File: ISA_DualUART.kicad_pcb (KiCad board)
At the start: 2 copper layers, 176.5 x 90.2 mm, 74 parts, among them J1 ISA BUS, J10 Parallel Port, J2 ADDR_IRQ, J3 UART1_SEL, J4 UART2_SEL, J6 Serial 2 IDC, J7 Serial 1 DB9, J9 Parport IRQ Select, U1 74LS138, U11 74LS30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

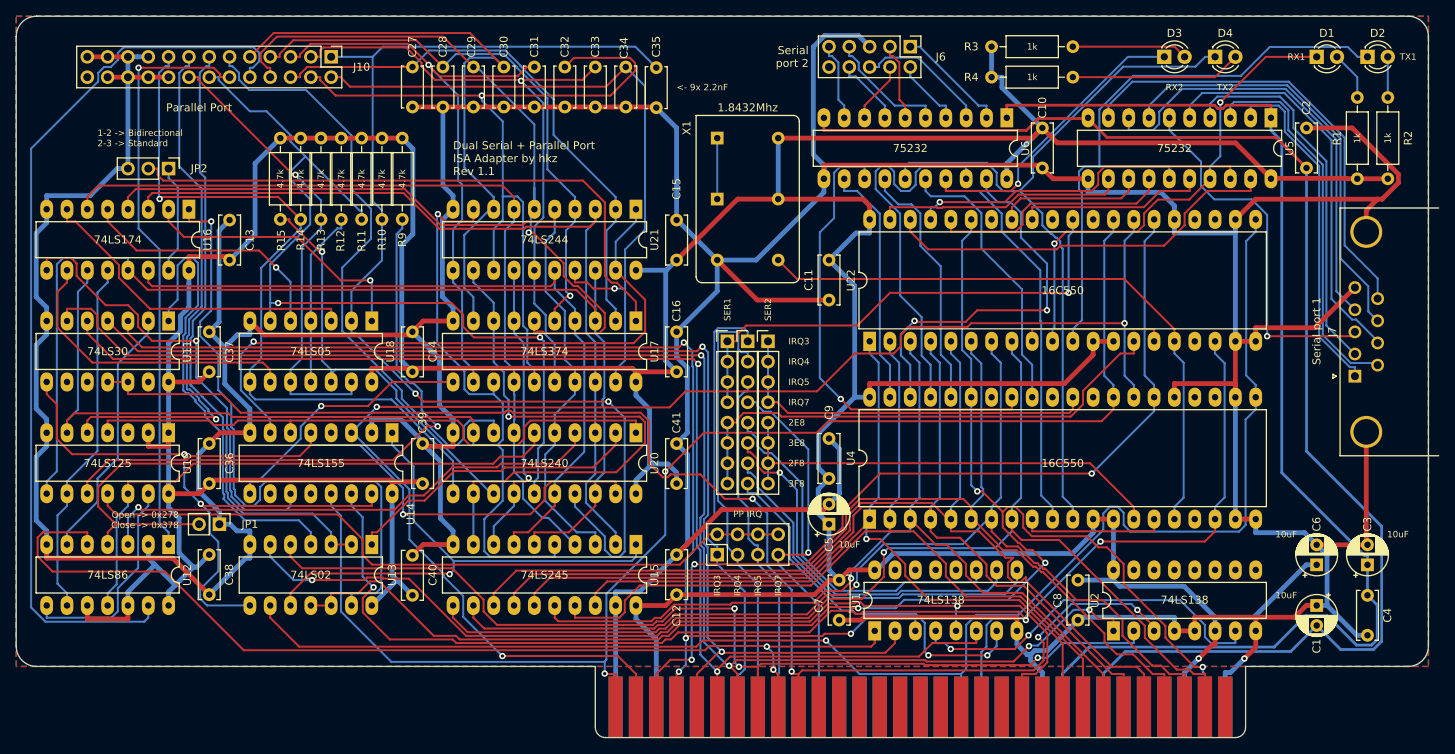
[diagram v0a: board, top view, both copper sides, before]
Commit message: Slightly better silkscreen
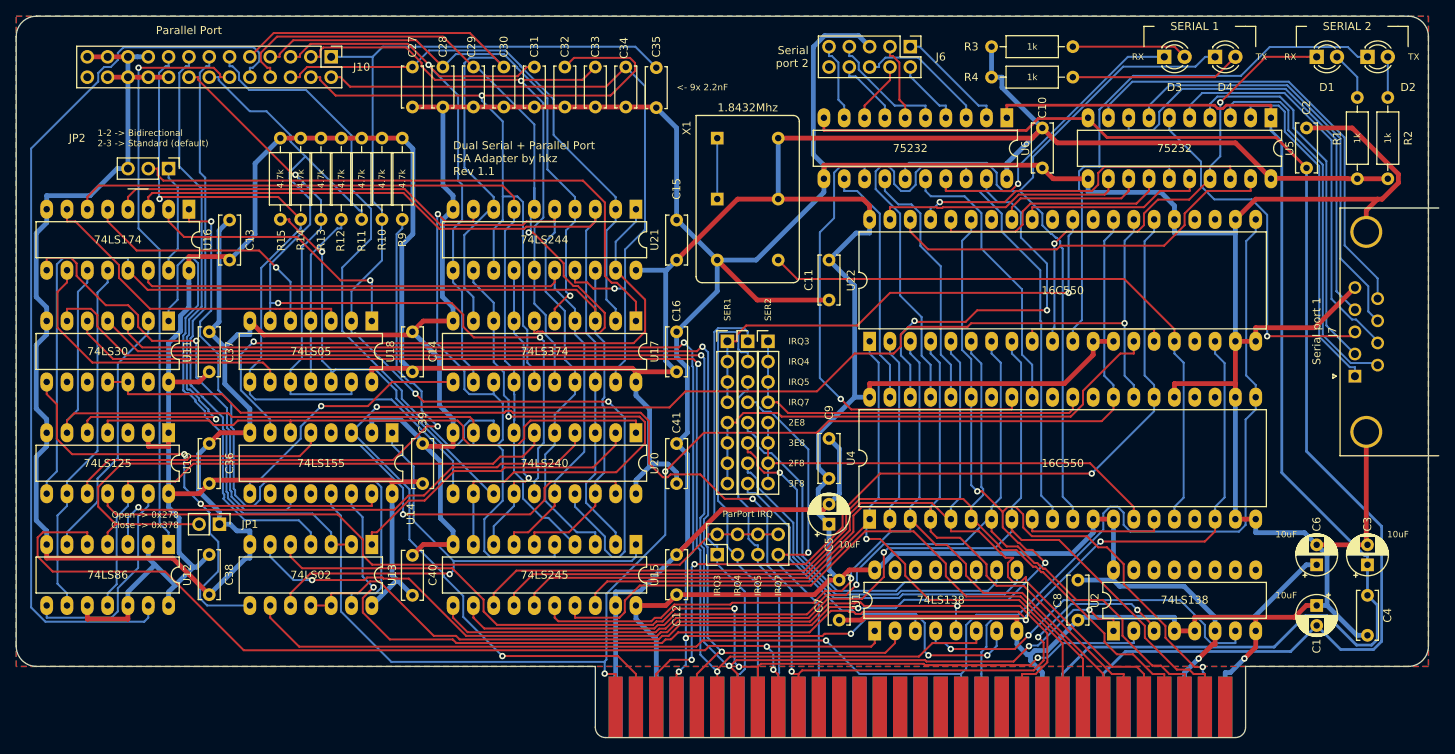
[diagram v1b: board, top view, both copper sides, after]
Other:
- board text added: "1-2 -> Bidirectional 2-3 -> Standard (default)"
- board text added: "ParPort IRQ"
- board text added: "RX"
- board text added: "SERIAL 1"
- board text added: "SERIAL 2"
- board text added: "TX"
- board text removed: "1-2 -> Bidirectional 2-3 -> Standard"
- board text removed: "PP IRQ"
- board text removed: "RX1"
- board text removed: "RX2"
- board text removed: "TX1"
- board text removed: "TX2"
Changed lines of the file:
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@@
   (general
     (thickness 1.6)
-    (drawings 76)
+    (drawings 89)
     (tracks 2452)
     (zones 0)
@@
   (page A3)
   (layers
-    (0 F.Cu signal)
-    (31 B.Cu signal)
+    (0 F.Cu signal hide)
+    (31 B.Cu signal hide)
     (32 B.Adhes user)
     (33 F.Adhes user)
@@
     (descr "Through hole straight pin header, 1x03, 2.54mm pitch, single row")
     (tags "Through hole pin header THT 1x03 2.54mm single row")
-    (fp_text reference JP2 (at 0 -3.81) (layer F.SilkS)
+    (fp_text reference JP2 (at -3.81 11.43) (layer F.SilkS)
       (effects (font (size 1 1) (thickness 0.15)))
     )
@@
     (descr "LED, diameter 3.0mm, 2 pins")
     (tags "LED diameter 3.0mm 2 pins")
-    (fp_text reference D4 (at 1.27 -2.96) (layer F.SilkS)
+    (fp_text reference D4 (at 1.27 3.81) (layer F.SilkS)
       (effects (font (size 1 1) (thickness 0.15)))
     )
@@
     (descr "LED, diameter 3.0mm, 2 pins")
     (tags "LED diameter 3.0mm 2 pins")
-    (fp_text reference D3 (at 1.27 -2.96) (layer F.SilkS)
+    (fp_text reference D3 (at 1.27 3.81) (layer F.SilkS)
       (effects (font (size 1 1) (thickness 0.15)))
     )
@@
     (descr "LED, diameter 3.0mm, 2 pins")
     (tags "LED diameter 3.0mm 2 pins")
-    (fp_text reference D2 (at 1.27 -2.96) (layer F.SilkS)
+    (fp_text reference D2 (at 5.08 3.81) (layer F.SilkS)
       (effects (font (size 1 1) (thickness 0.15)))
     )
@@
     (descr "LED, diameter 3.0mm, 2 pins")
     (tags "LED diameter 3.0mm 2 pins")
-    (fp_text reference D1 (at 1.27 -2.96) (layer F.SilkS)
+    (fp_text reference D1 (at 1.27 3.81) (layer F.SilkS)
       (effects (font (size 1 1) (thickness 0.15)))
     )
@@
     )
   )
+  (gr_line (start 152.4 134.62) (end 154.94 134.62) (layer F.SilkS) (width 0.12))
+  (gr_line (start 292.1 114.3) (end 290.83 114.3) (layer F.SilkS) (width 0.12))
+  (gr_line (start 311.15 114.3) (end 309.88 114.3) (layer F.SilkS) (width 0.12))
+  (gr_line (start 312.42 114.3) (end 311.15 114.3) (layer F.SilkS) (width 0.12))
+  (gr_line (start 312.42 116.84) (end 312.42 114.3) (layer F.SilkS) (width 0.12))
+  (gr_line (start 298.45 114.3) (end 299.72 114.3) (layer F.SilkS) (width 0.12))
+  (gr_line (start 298.45 116.84) (end 298.45 114.3) (layer F.SilkS) (width 0.12))
+  (gr_line (start 293.37 114.3) (end 292.1 114.3) (layer F.SilkS) (width 0.12))
+  (gr_line (start 293.37 116.84) (end 293.37 114.3) (layer F.SilkS) (width 0.12))
+  (gr_line (start 279.4 114.3) (end 280.67 114.3) (layer F.SilkS) (width 0.12))
+  (gr_line (start 279.4 116.84) (end 279.4 114.3) (layer F.SilkS) (width 0.12))
+  (gr_text "SERIAL 2" (at 304.8 114.3) (layer F.SilkS)
+    (effects (font (size 1 1) (thickness 0.25)))
+  )
+  (gr_text "SERIAL 1" (at 285.75 114.3) (layer F.SilkS)
+    (effects (font (size 1 1) (thickness 0.25)))
+  )
   (gr_text 10uF (at 297.18 185.42) (layer F.SilkS)
     (effects (font (size 0.8 0.8) (thickness 0.15)))
@@
     (effects (font (size 1 1) (thickness 0.15)))
   )
-  (gr_text "1-2 -> Bidirectional\n2-3 -> Standard" (at 148.59 128.27) (layer F.SilkS)
+  (gr_text "1-2 -> Bidirectional\n2-3 -> Standard (default)" (at 148.59 128.27) (layer F.SilkS)
     (effects (font (size 0.8 0.8) (thickness 0.15)) (justify left))
   )
@@
     (effects (font (size 0.8 0.8) (thickness 0.15)) (justify right))
   )
-  (gr_text "PP IRQ" (at 229.87 175.26) (layer F.SilkS)
+  (gr_text "ParPort IRQ" (at 229.87 175.26) (layer F.SilkS)
     (effects (font (size 0.8 0.8) (thickness 0.15)))
   )
@@
     (effects (font (size 0.8 0.8) (thickness 0.15)) (justify right))
   )
-  (gr_text RX1 (at 298.45 118.11) (layer F.SilkS)
-    (effects (font (size 0.8 0.8) (thickness 0.15)))
+  (gr_text RX (at 298.45 118.11) (layer F.SilkS)
+    (effects (font (size 0.8 0.8) (thickness 0.15)) (justify right))
   )
-  (gr_text TX1 (at 312.42 118.11) (layer F.SilkS)
-    (effects (font (size 0.8 0.8) (thickness 0.15)))
+  (gr_text TX (at 312.42 118.11) (layer F.SilkS)
+    (effects (font (size 0.8 0.8) (thickness 0.15)) (justify left))
   )
-  (gr_text TX2 (at 289.56 121.92) (layer F.SilkS)
-    (effects (font (size 0.8 0.8) (thickness 0.15)))
+  (gr_text TX (at 293.37 118.11) (layer F.SilkS)
+    (effects (font (size 0.8 0.8) (thickness 0.15)) (justify left))
   )
-  (gr_text RX2 (at 283.21 121.92) (layer F.SilkS)
-    (effects (font (size 0.8 0.8) (thickness 0.15)))
+  (gr_text RX (at 279.4 118.11) (layer F.SilkS)
+    (effects (font (size 0.8 0.8) (thickness 0.15)) (justify right))
   )
   (gr_text "Serial\nport 2" (at 237.49 118.11) (layer F.SilkS)
     (effects (font (size 1 1) (thickness 0.25)) (justify right))
   )
-  (gr_text "Parallel Port" (at 161.29 124.46) (layer F.SilkS)
+  (gr_text "Parallel Port" (at 160.02 114.8) (layer F.SilkS)
     (effects (font (size 1 1) (thickness 0.25)))
   )

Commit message: Rerouted card
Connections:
- J10 pad 10: /~PARPORT_ACK -> GND
- J10 pad 11: /PARPORT_BUSY -> /PARPORT_DATA4
- J10 pad 12: /PARPORT_PE -> GND
- J10 pad 13: /PARPORT_SLCT -> /PARPORT_DATA5
- J10 pad 14: /~PARPORT_AUTOFD -> GND
- J10 pad 15: /~PARPORT_ERROR -> /PARPORT_DATA6
- J10 pad 16: /~PARPORT_INIT -> GND
- J10 pad 17: /~PARPORT_SLCTIN -> /PARPORT_DATA7
- J10 pad 19: GND -> /~PARPORT_ACK
- J10 pad 2: /PARPORT_DATA0 -> GND
- J10 pad 20: GND -> /~PARPORT_SLCTIN
- J10 pad 21: GND -> /PARPORT_BUSY
- J10 pad 22: GND -> /~PARPORT_INIT
- J10 pad 23: GND -> /PARPORT_PE
- J10 pad 24: GND -> /~PARPORT_ERROR
- J10 pad 25: GND -> /PARPORT_SLCT
- J10 pad 26: (no net) -> /~PARPORT_AUTOFD
- J10 pad 3: /PARPORT_DATA1 -> /PARPORT_DATA0
- J10 pad 4: /PARPORT_DATA2 -> GND
- J10 pad 5: /PARPORT_DATA3 -> /PARPORT_DATA1
- J10 pad 6: /PARPORT_DATA4 -> GND
- J10 pad 7: /PARPORT_DATA5 -> /PARPORT_DATA2
- J10 pad 8: /PARPORT_DATA6 -> GND
- J10 pad 9: /PARPORT_DATA7 -> /PARPORT_DATA3
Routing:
- net /PARPORT_BD3: track 147.8 -> 194.1 mm
- net GND: track 798.4 -> 754.4 mm, vias 1 -> 0
- net /PARPORT_BD7: track 71.4 -> 41.8 mm
- net /PARPORT_DATA5: track 71.1 -> 97.2 mm
- net /A2: track 112.9 -> 137.8 mm, vias 3 -> 2
- net /PARPORT_PE: track 73.2 -> 98.1 mm, vias 1 -> 0
- net /PARPORT_DATA1: track 79.6 -> 102.5 mm, vias 1 -> 0
- net /~PARPORT_ACK: track 113.4 -> 91.6 mm
- net /~PARPORT_INIT: track 58.0 -> 78.8 mm, vias 1 -> 0
- net /~DTR_2: track 59.2 -> 38.6 mm
- net /PARPORT_SLCT: track 77.6 -> 98.0 mm, vias 0 -> 1
- net /PARPORT_DATA4: track 68.9 -> 88.8 mm
- net /A1: track 184.0 -> 164.4 mm
- net Net-(JP1-Pad2): track 93.0 -> 74.2 mm, vias 1 -> 2
- net /PARPORT_BUSY: track 76.6 -> 95.4 mm
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
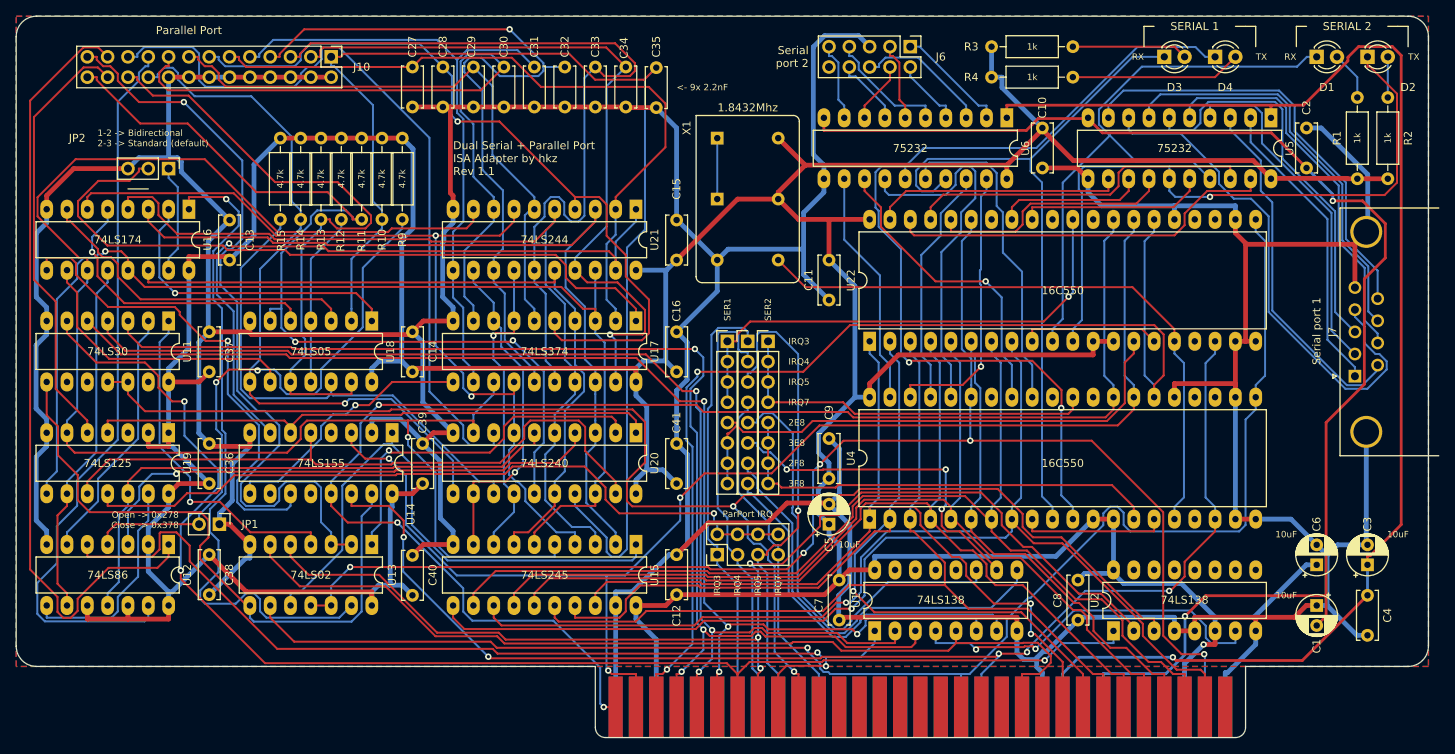
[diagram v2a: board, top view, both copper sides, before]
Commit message: Changed organization of parport connector
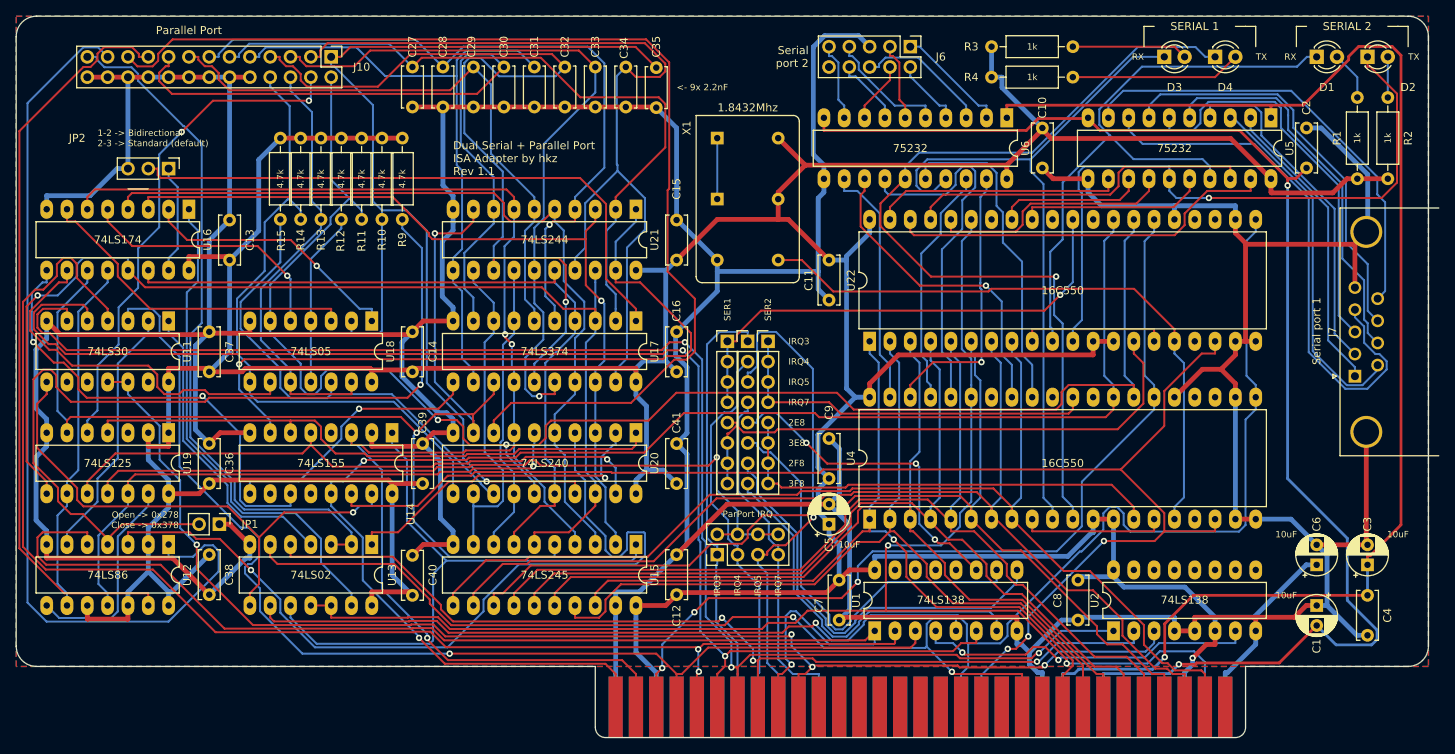
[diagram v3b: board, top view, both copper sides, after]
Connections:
- J10 pad 2: GND -> /~PARPORT_AUTOFD
- J10 pad 20: /~PARPORT_SLCTIN -> GND
- J10 pad 22: /~PARPORT_INIT -> GND
- J10 pad 24: /~PARPORT_ERROR -> GND
- J10 pad 26: /~PARPORT_AUTOFD -> GND
- J10 pad 4: GND -> /~PARPORT_ERROR
- J10 pad 6: GND -> /~PARPORT_INIT
- J10 pad 8: GND -> /~PARPORT_SLCTIN
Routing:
- net /PARPORT_BD3: track 194.1 -> 150.2 mm, vias 1 -> 2
- net /PARPORT_BUSY: track 95.4 -> 139.1 mm
- net Net-(U12-Pad3): track 66.0 -> 105.5 mm
- net Net-(JP1-Pad2): track 74.2 -> 111.6 mm, vias 2 -> 1
- net /~PARPORT_AUTOFD: track 118.7 -> 89.3 mm
- net /A1: track 164.4 -> 193.6 mm, vias 3 -> 1
- net /A4: track 144.7 -> 173.1 mm, vias 3 -> 2
- net /A2: track 137.8 -> 111.0 mm, vias 2 -> 3
- net /~PARPORT_INIT: track 78.8 -> 55.0 mm
- net /A8: track 124.1 -> 147.3 mm, vias 2 -> 1
- net /A9: track 186.5 -> 164.5 mm, vias 2 -> 4
- net /A7: track 143.8 -> 122.5 mm
- net /~PARPORT_RESET: track 83.5 -> 63.0 mm, vias 1 -> 0
- net GND: track 754.4 -> 773.3 mm
- net /A5: track 155.6 -> 174.3 mm, vias 4 -> 2
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
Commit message: Invert IRQ sensing to conform to AT specs
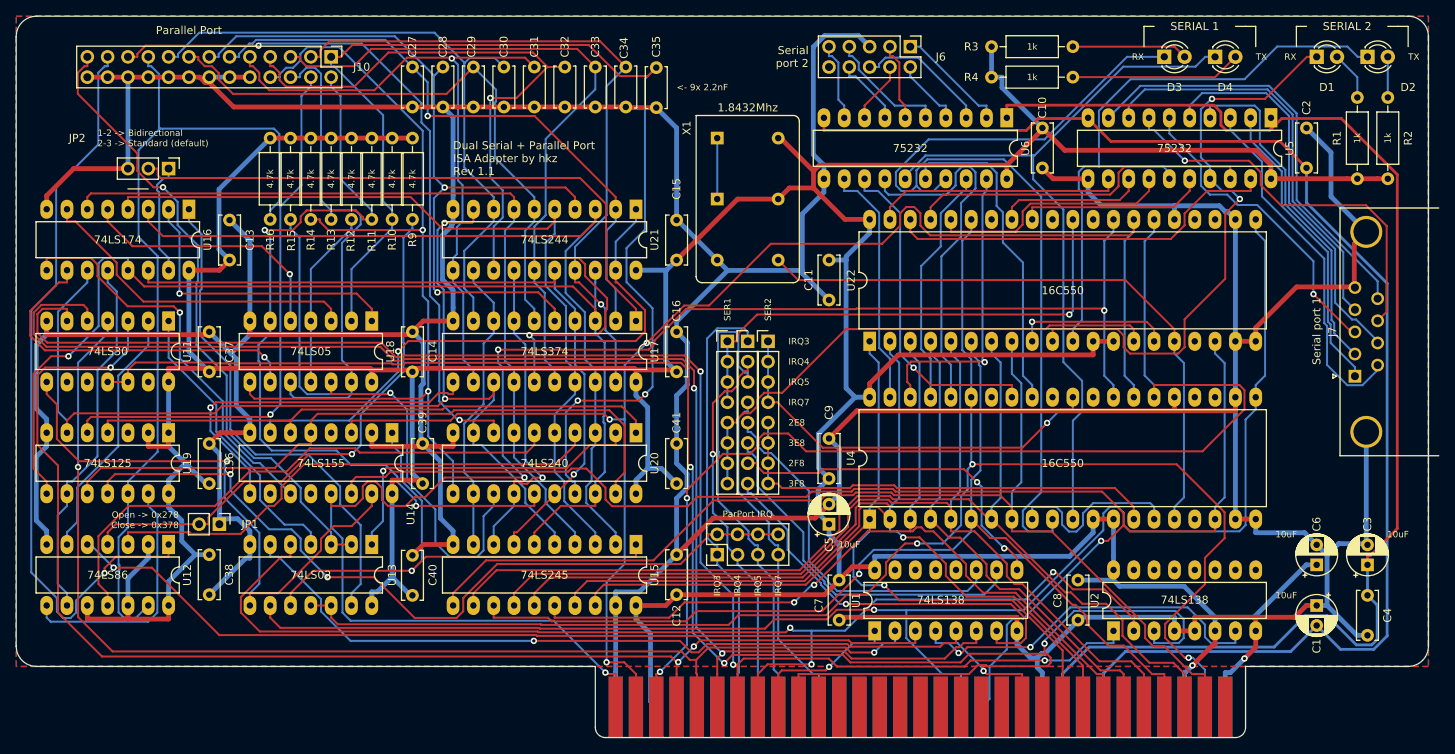
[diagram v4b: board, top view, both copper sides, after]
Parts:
- added R16: 4.7k, Resistor_THT:R_Axial_DIN0207_L6.3mm_D2.5mm_P10.16mm_Horizontal, F.Cu at (170.2, 128.3)
- moved R12 1.27 mm to (180.3, 128.3)
- moved R13 1.27 mm to (177.8, 128.3)
- moved R15 1.27 mm to (172.7, 128.3)
- moved R9 1.27 mm to (188.0, 128.3)
- moved R10 1.27 mm to (185.4, 128.3)
- moved R11 1.27 mm to (182.9, 128.3)
- moved R14 1.27 mm to (175.3, 128.3)
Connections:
- U19 pad 12: /PARPORT_IRQ -> /~PARPORT_ACK
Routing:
- net /A9: track 164.5 -> 221.7 mm, vias 4 -> 3
- net /PARPORT_BUSY: track 139.1 -> 88.2 mm, vias 0 -> 2
- net Net-(JP1-Pad2): track 111.6 -> 69.1 mm
- net Net-(U12-Pad3): track 105.5 -> 64.5 mm, vias 1 -> 0
- net /A2: track 111.0 -> 143.7 mm, vias 3 -> 2
- net /~PARPORT_SLCTIN: track 80.2 -> 111.7 mm, vias 0 -> 2
- net /SIN_2: track 89.5 -> 116.6 mm
- net /A0: track 181.3 -> 207.1 mm, vias 2 -> 4
- net GND: track 773.3 -> 798.9 mm, vias 0 -> 1
- net /A7: track 122.5 -> 147.3 mm
- net /A8: track 147.3 -> 122.7 mm, vias 1 -> 2
- net /PARPORT_DATA0: track 110.7 -> 86.4 mm, vias 0 -> 1
- net /A3: track 142.7 -> 165.2 mm, vias 1 -> 3
- net /A4: track 173.1 -> 151.7 mm
- net /PARPORT_PE: track 114.5 -> 95.1 mm, vias 0 -> 1
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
